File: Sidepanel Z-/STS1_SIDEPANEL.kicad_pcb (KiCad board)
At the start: 2 copper layers, 98 x 98 mm, 62 parts, among them IC1 TMP112AQDRLRQ1, J1 Conn_01x08, J3 Conn_02x02_Odd_Even, U1 GUVA-C32SM, U11 INA180A4, U12 INA180A4

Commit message: added the flex pcb
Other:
- board text removed: "C1"
- board text removed: "C2"
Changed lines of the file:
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@@
     (property "Sheetname" "SolarMPPT")
     (attr smd)
-    (fp_text reference "L_IN1" (at 0 0 270) (layer "B.SilkS")
+    (fp_text reference "L_IN1" (at 0 0) (layer "B.SilkS")
       (effects (font (size 1.27 1.27) (thickness 0.254)) (justify mirror))
     )
@@
     (property "Sheetname" "SolarMPPT")
     (attr smd)
-    (fp_text reference "RF12" (at 0 -3.25) (layer "B.SilkS")
+    (fp_text reference "RF12" (at -0.2162 -3.25) (layer "B.SilkS")
       (effects (font (size 1 1) (thickness 0.15)) (justify mirror))
     )
@@
     (property "Sheetname" "Sensors")
     (attr smd)
-    (fp_text reference "C1" (at 0 1.43) (layer "B.SilkS")
+    (fp_text reference "C1" (at 2.516 0.0784) (layer "B.SilkS")
       (effects (font (size 1 1) (thickness 0.15)) (justify mirror))
     )
@@
     (property "Sheetname" "Sensors")
     (attr smd)
-    (fp_text reference "C2" (at 0 -2.25) (layer "B.SilkS")
+    (fp_text reference "C2" (at -2.516 0.1286) (layer "B.SilkS")
       (effects (font (size 1 1) (thickness 0.15)) (justify mirror))
     )
@@
     (property "Sheetname" "Sensors")
     (attr smd)
-    (fp_text reference "IC1" (at 0 1.7 180) (layer "B.SilkS")
+    (fp_text reference "IC1" (at -0.0776 1.7796 180) (layer "B.SilkS")
       (effects (font (size 1 1) (thickness 0.15)) (justify mirror))
     )
@@
     (property "Sheetname" "SolarMPPT")
     (attr smd)
-    (fp_text reference "RF22" (at 0.237258 -3.75) (layer "B.SilkS")
+    (fp_text reference "RF22" (at -0.267 -3.5992) (layer "B.SilkS")
       (effects (font (size 1 1) (thickness 0.15)) (justify mirror))
     )
@@
     (property "Sheetname" "SolarMPPT")
     (attr smd)
-    (fp_text reference "DOUT2" (at -0.702 3.719) (layer "B.SilkS")
+    (fp_text reference "DOUT2" (at 0.055 -2.0756) (layer "B.SilkS")
       (effects (font (size 1.27 1.27) (thickness 0.254)) (justify mirror))
     )
@@
     (property "Sheetname" "SolarMPPT")
     (attr smd)
-    (fp_text reference "R51" (at 0 1.43) (layer "B.SilkS")
+    (fp_text reference "R51" (at 2.5908 0) (layer "B.SilkS")
       (effects (font (size 1 1) (thickness 0.15)) (justify mirror))
     )
@@
     (property "Sheetname" "SolarMPPT")
     (attr smd)
-    (fp_text reference "COUT12" (at 0 -3) (layer "B.SilkS")
+    (fp_text reference "COUT12" (at 0.0454 -1.9004) (layer "B.SilkS")
       (effects (font (size 1 1) (thickness 0.15)) (justify mirror))
     )
@@
     (property "Sheetname" "SolarMPPT")
     (attr smd)
-    (fp_text reference "CF2" (at 3.25 0 90) (layer "B.SilkS")
+    (fp_text reference "CF2" (at 3.158 0.4334 90) (layer "B.SilkS")
       (effects (font (size 1 1) (thickness 0.15)) (justify mirror))
     )
@@
     (property "Sheetname" "SolarMPPT")
     (attr smd)
-    (fp_text reference "C_CUR21" (at 5 0 90) (layer "B.SilkS")
+    (fp_text reference "C_CUR21" (at -5.2448 0.1302 90) (layer "B.SilkS")
       (effects (font (size 1 1) (thickness 0.15)) (justify mirror))
     )
@@
     (property "Sheetname" "SolarMPPT")
     (attr smd)
-    (fp_text reference "DOUT1" (at -0.702 3.719 180) (layer "B.SilkS")
+    (fp_text reference "DOUT1" (at 1.5078 -2.0832 180) (layer "B.SilkS")
       (effects (font (size 1.27 1.27) (thickness 0.254)) (justify mirror))
     )
@@
     (property "Sheetname" "SolarMPPT")
     (attr smd)
-    (fp_text reference "MPPT1" (at 0 2.45 180) (layer "B.SilkS")
+    (fp_text reference "MPPT1" (at 0.1034 -1.8788 180) (layer "B.SilkS")
       (effects (font (size 1 1) (thickness 0.15)) (justify mirror))
     )
@@
     (property "Sheetname" "SolarMPPT")
     (attr smd)
-    (fp_text reference "C_CUR12" (at -5 0 90) (layer "B.SilkS")
+    (fp_text reference "C_CUR12" (at -1.4932 1.5748 90) (layer "B.SilkS")
       (effects (font (size 1 1) (thickness 0.15)) (justify mirror))
     )
@@
     (property "Sheetname" "SolarMPPT")
     (attr smd)
-    (fp_text reference "CF1" (at 3.25 0 90) (layer "B.SilkS")
+    (fp_text reference "CF1" (at 2.7948 0.2738 90) (layer "B.SilkS")
       (effects (font (size 1 1) (thickness 0.15)) (justify mirror))
     )
@@
     (property "Sheetname" "SolarMPPT")
     (attr smd)
-    (fp_text reference "RF21" (at 0.237258 -3.75) (layer "B.SilkS")
+    (fp_text reference "RF21" (at -0.071 -3.6424) (layer "B.SilkS")
       (effects (font (size 1 1) (thickness 0.15)) (justify mirror))
     )
@@
     (property "Sheetname" "SolarMPPT")
     (attr smd)
-    (fp_text reference "C_IN2" (at 0.75 -1.5 90) (layer "B.SilkS")
+    (fp_text reference "C_IN2" (at 0.4784 -1.4446 90) (layer "B.SilkS")
       (effects (font (size 1 1) (thickness 0.15)) (justify mirror))
     )
@@
     (property "Sheetname" "SolarMPPT")
     (attr smd)
-    (fp_text reference "C_42" (at 0 1.43) (layer "B.SilkS")
+    (fp_text reference "C_42" (at -0.147 -1.5256) (layer "B.SilkS")
       (effects (font (size 1 1) (thickness 0.15)) (justify mirror))
     )
@@
     (property "Sheetname" "SolarMPPT")
     (attr smd)
-    (fp_text reference "C_CUR11" (at -5 0 90) (layer "B.SilkS")
+    (fp_text reference "C_CUR11" (at 5.2956 -0.0006 90) (layer "B.SilkS")
       (effects (font (size 1 1) (thickness 0.15)) (justify mirror))
     )
@@
     (property "Sheetname" "SolarMPPT")
     (attr smd)
-    (fp_text reference "L_IN2" (at 0 0 90) (layer "B.SilkS")
+    (fp_text reference "L_IN2" (at 0 0 180) (layer "B.SilkS")
       (effects (font (size 1.27 1.27) (thickness 0.254)) (justify mirror))
     )
@@
     (property "Sheetname" "SolarMPPT")
     (attr smd)
-    (fp_text reference "CUR1" (at 0 3.4 180) (layer "B.SilkS")
+    (fp_text reference "CUR1" (at -0.0326 -0.3084 270) (layer "B.SilkS")
       (effects (font (size 1 1) (thickness 0.15)) (justify mirror))
     )
@@
     (property "Sheetname" "SolarMPPT")
     (attr smd)
-    (fp_text reference "R31" (at 0 1.43) (layer "B.SilkS")
+    (fp_text reference "R31" (at 0.0074 -1.5688) (layer "B.SilkS")
       (effects (font (size 1 1) (thickness 0.15)) (justify mirror))
     )
@@
     (property "Sheetname" "SolarMPPT")
     (attr smd)
-    (fp_text reference "MPPT2" (at 0 2.45) (layer "B.SilkS")
+    (fp_text reference "MPPT2" (at 0.0962 -0.144) (layer "B.SilkS")
       (effects (font (size 1 1) (thickness 0.15)) (justify mirror))
     )
@@
     (property "Sheetname" "")
     (attr smd)
-    (fp_text reference "J1" (at -2.65 4.43 180) (layer "B.SilkS")
+    (fp_text reference "J1" (at -3.0988 3.9844 180) (layer "B.SilkS")
       (effects (font (size 1 1) (thickness 0.15)) (justify mirror))
     )
@@
     (property "Sheetname" "SolarMPPT")
     (attr smd)
-    (fp_text reference "R32" (at 0 1.43) (layer "B.SilkS")
+    (fp_text reference "R32" (at -0.0362 -1.6272) (layer "B.SilkS")
       (effects (font (size 1 1) (thickness 0.15)) (justify mirror))
     )
@@
     (property "Sheetname" "SolarMPPT")
     (attr smd)
-    (fp_text reference "RS2" (at 0 3.25) (layer "B.SilkS")
-      (effects (font (size 1 1) (thickness 0.15)) (justify mirror))
+    (fp_text reference "RS2" (at -0.0962 -1.1756) (layer "B.SilkS")
+      (effects (font (size 0.9 0.9) (thickness 0.15)) (justify mirror))
     )
     (fp_text value "0R01" (at 0 -1.43) (layer "B.Fab")
@@
     (property "Sheetname" "SolarMPPT")
     (attr smd)
-    (fp_text reference "C_41" (at 0 1.43) (layer "B.SilkS")
-      (effects (font (size 1 1) (thickness 0.15)) (justify mirror))
+    (fp_text reference "C_41" (at 0.9634 -2.1276 90) (layer "B.SilkS")
+      (effects (font (size 0.9 0.9) (thickness 0.15)) (justify mirror))
     )
     (fp_text value "100n" (at 0 -1.43) (layer "B.Fab")
@@
     (property "Sheetname" "SolarMPPT")
     (attr smd)
-    (fp_text reference "C_CUR22" (at 5 0 90) (layer "B.SilkS")
+    (fp_text reference "C_CUR22" (at 1.4424 1.6002 90) (layer "B.SilkS")
       (effects (font (size 1 1) (thickness 0.15)) (justify mirror))
     )
@@
   (gr_arc (start 130.5 89) (mid 131.707107 89.5) (end 130.5 90) (layer "Edge.Cuts") (width 0.1))
   (gr_arc (start 119.5 90) (mid 118.292893 89.5) (end 119.5 89) (layer "Edge.Cuts") (width 0.1))
-  (gr_text "C2" (at 101.25 104.25 -180) (layer "B.SilkS")
-    (effects (font (size 1 1) (thickness 0.15)) (justify mirror))
-  )
   (gr_text "Z-" (at 86.9 42.51) (layer "B.SilkS")
     (effects (font (size 1 1) (thickness 0.15)))
   )
-  (gr_text "C1" (at 97 104.18) (layer "B.SilkS")
-    (effects (font (size 1 1) (thickness 0.15)) (justify mirror))
-  )
   (gr_text "98 mm x 98 mm" (at 108.49 38.192) (layer "F.SilkS")

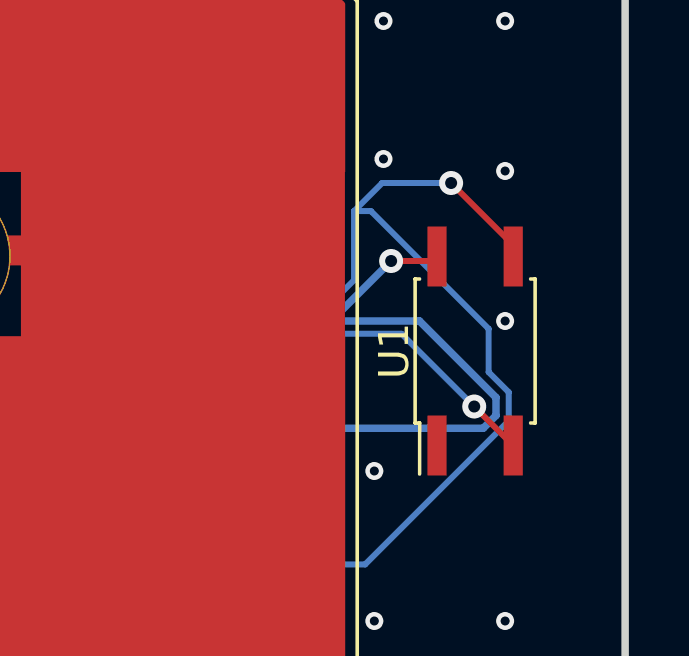
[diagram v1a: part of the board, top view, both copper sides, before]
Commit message: fix for the issues: #19, #18 moved some components from the edge away to avoid collisions with the new structure
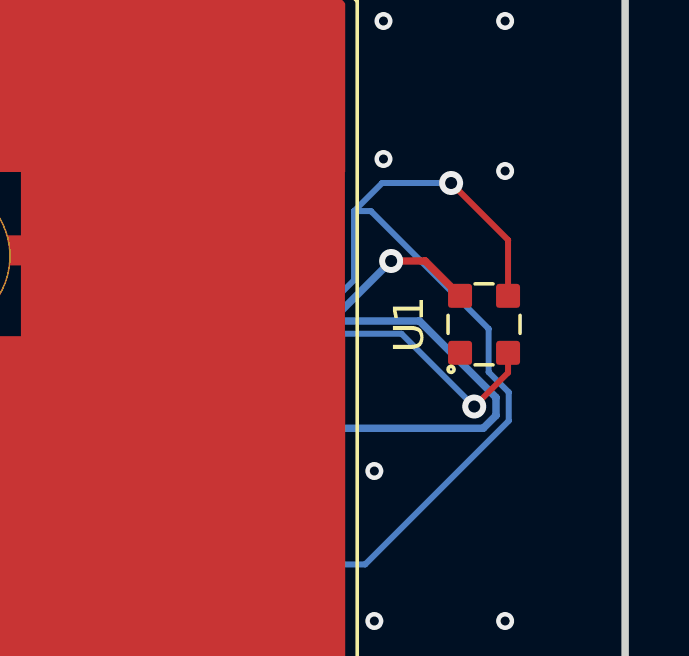
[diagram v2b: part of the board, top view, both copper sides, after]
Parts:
- U1: footprint Package_SO:SO-4_4.4x3.6mm_P2.54mm -> STS_UV:OLGA 2mm x 2,3mm
- moved U1 0.94 mm to (169.3, 69.6)
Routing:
- net /SCL: track 69.6 -> 70.8 mm
- net /+3V3: track 63.0 -> 64.2 mm
- net GND: vias 110 -> 109
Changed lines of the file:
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@@
     )
   )
-  (footprint "Package_SO:SO-4_4.4x3.6mm_P2.54mm" (layer "F.Cu")
-    (at 169 70.5 90)
-    (descr "4-Lead Plastic Small Outline (SO), see https://www.elpro.org/de/index.php?controller=attachment&id_attachment=339")
-    (tags "SO SOIC 2.54")
+  (footprint "STS_UV:OLGA 2mm x 2,3mm" (layer "F.Cu")
+    (at 169.2976 69.6118 90)
     (property "Sheetfile" "Sensors.kicad_sch")
     (property "Sheetname" "Sensors")
     (attr smd)
-    (fp_text reference "U1" (at 0 -2.7 90) (layer "F.SilkS")
+    (fp_text reference "U1" (at 0 -2.5 90 unlocked) (layer "F.SilkS")
       (effects (font (size 1 1) (thickness 0.15)))
     )
-    (fp_text value "GUVA-C32SM" (at 0 2.8 90) (layer "F.Fab")
+    (fp_text value "GUVA-C32SM" (at 0 2.5 90 unlocked) (layer "F.Fab")
       (effects (font (size 1 1) (thickness 0.15)))
     )
-    (fp_text user "${REFERENCE}" (at 0 -0.065 90) (layer "F.Fab")
+    (fp_text user "${REFERENCE}" (at 0.2 5.6 90 unlocked) (layer "F.Fab") hide
       (effects (font (size 1 1) (thickness 0.15)))
     )
-    (fp_line (start 2.4 -2) (end 2.4 -1.85) (layer "F.SilkS") (width 0.12))
-    (fp_line (start 2.4 2) (end -2.4 2) (layer "F.SilkS") (width 0.12))
-    (fp_line (start 2.4 1.85) (end 2.4 2) (layer "F.SilkS") (width 0.12))
-    (fp_line (start -2.4 -2) (end 2.4 -2) (layer "F.SilkS") (width 0.12))
-    (fp_line (start -2.4 -1.85) (end -2.4 -2) (layer "F.SilkS") (width 0.12))
-    (fp_line (start -2.4 2) (end -2.4 1.85) (layer "F.SilkS") (width 0.12))
-    (fp_line (start -2.4 -1.85) (end -4.1 -1.85) (layer "F.SilkS") (width 0.12))
-    (fp_line (start -4.4 -2.05) (end 4.4 -2.05) (layer "F.CrtYd") (width 0.05))
-    (fp_line (start 4.4 2.05) (end 4.4 -2.05) (layer "F.CrtYd") (width 0.05))
-    (fp_line (start 4.4 2.05) (end -4.4 2.05) (layer "F.CrtYd") (width 0.05))
-    (fp_line (start -4.4 -2.05) (end -4.4 2.05) (layer "F.CrtYd") (width 0.05))
-    (fp_line (start 2.2 -1.8) (end 2.2 1.8) (layer "F.Fab") (width 0.12))
-    (fp_line (start -1.4 -1.8) (end 2.2 -1.8) (layer "F.Fab") (width 0.12))
-    (fp_line (start -2.2 1.8) (end -2.2 -1) (layer "F.Fab") (width 0.12))
-    (fp_line (start 2.2 1.8) (end -2.2 1.8) (layer "F.Fab") (width 0.12))
-    (fp_line (start -2.2 -1) (end -1.4 -1.8) (layer "F.Fab") (width 0.12))
-    (pad "1" smd rect (at -3.15 -1.27 90) (size 2 0.64) (layers "F.Cu" "F.Paste" "F.Mask")
+    (fp_line (start -0.3 -1.2) (end 0.3 -1.2) (layer "F.SilkS") (width 0.12))
+    (fp_line (start -1.35 0.3) (end -1.35 -0.3) (layer "F.SilkS") (width 0.12))
+    (fp_line (start 1.35 0.3) (end 1.35 -0.3) (layer "F.SilkS") (width 0.12))
+    (fp_line (start -0.3 1.2) (end 0.3 1.2) (layer "F.SilkS") (width 0.12))
+    (fp_circle (center -1.5 -1.1) (end -1.5 -1.2) (layer "F.SilkS") (width 0.12) (fill none))
+    (fp_line (start 1.6 -1.5) (end -1.6 -1.5) (layer "F.CrtYd") (width 0.05))
+    (fp_line (start -1.6 1.5) (end 1.6 1.5) (layer "F.CrtYd") (width 0.05))
+    (fp_line (start -1.6 1.5) (end -1.6 -1.5) (layer "F.CrtYd") (width 0.05))
+    (fp_line (start 1.6 -1.5) (end 1.6 1.5) (layer "F.CrtYd") (width 0.05))
+    (fp_line (start 1.15 1) (end 1.15 -1) (layer "F.Fab") (width 0.1))
+    (fp_line (start -0.6 0.3) (end 0.6 0.3) (layer "F.Fab") (width 0.1))
+    (fp_line (start -0.4 -0.3) (end -0.4 -0.5) (layer "F.Fab") (width 0.1))
+    (fp_line (start -0.2 -0.1) (end -0.2 0.7) (layer "F.Fab") (width 0.1))
+    (fp_line (start -1.15 1) (end 1.15 1) (layer "F.Fab") (width 0.1))
+    (fp_line (start 0.2 0.7) (end 0.2 -0.1) (layer "F.Fab") (width 0.1))
+    (fp_line (start -1.15 -1) (end -1.15 1) (layer "F.Fab") (width 0.1))
+    (fp_line (start -0.4 -0.3) (end -0.1 -0.6) (layer "F.Fab") (width 0.1))
+    (fp_line (start 0.1 -0.3) (end 0.1 -0.5) (layer "F.Fab") (width 0.1))
+    (fp_line (start -0.2 0.3) (end 0.2 0.7) (layer "F.Fab") (width 0.1))
+    (fp_line (start 0.2 -0.1) (end -0.2 0.3) (layer "F.Fab") (width 0.1))
+    (fp_line (start 1.15 -1) (end -1.15 -1) (layer "F.Fab") (width 0.1))
+    (fp_line (start 0.1 -0.3) (end 0.3 -0.3) (layer "F.Fab") (width 0.1))
+    (fp_line (start 0.1 -0.3) (end 0.4 -0.6) (layer "F.Fab") (width 0.1))
+    (fp_line (start -0.4 -0.3) (end -0.2 -0.3) (layer "F.Fab") (width 0.1))
+    (pad "1" smd roundrect (at -0.95 -0.8 270) (size 0.8 0.8) (layers "F.Cu" "F.Paste" "F.Mask") (roundrect_rratio 0.125)
       (net 1 "GND") (pinfunction "GND") (pintype "power_in"))
-    (pad "2" smd rect (at -3.15 1.27 90) (size 2 0.64) (layers "F.Cu" "F.Paste" "F.Mask")
+    (pad "2" smd roundrect (at -0.95 0.8 270) (size 0.8 0.8) (layers "F.Cu" "F.Paste" "F.Mask") (roundrect_rratio 0.125)
       (net 6 "/SDA") (pinfunction "SDA") (pintype "bidirectional"))
-    (pad "3" smd rect (at 3.15 1.27 90) (size 2 0.64) (layers "F.Cu" "F.Paste" "F.Mask")
+    (pad "3" smd roundrect (at 0.95 0.8 270) (size 0.8 0.8) (layers "F.Cu" "F.Paste" "F.Mask") (roundrect_rratio 0.125)
       (net 4 "/SCL") (pinfunction "SCL") (pintype "input"))
-    (pad "4" smd rect (at 3.15 -1.27 90) (size 2 0.64) (layers "F.Cu" "F.Paste" "F.Mask")
+    (pad "4" smd roundrect (at 0.95 -0.8 270) (size 0.8 0.8) (layers "F.Cu" "F.Paste" "F.Mask") (roundrect_rratio 0.125)
       (net 3 "/+3V3") (pinfunction "VCC") (pintype "power_in"))
-    (model "${KICAD6_3DMODEL_DIR}/Package_SO.3dshapes/SO-4_4.4x3.6mm_P2.54mm.wrl"
-      (offset (xyz 0 0 0))
-      (scale (xyz 1 1 1))
-      (rotate (xyz 0 0 0))
+    (model "C:/Users/Alex/Documents/KiCad/6.0/3dmodels/OLGA2x2,3.stp"
+      (offset (xyz 0 0 0))
+      (scale (xyz 1 1 1))
+      (rotate (xyz 90 -180 180))
     )
   )
@@
   (via (at 125 132.71) (size 0.6) (drill 0.3) (layers "F.Cu" "B.Cu") (free) (net 1))
   (via (at 165.64 74.5) (size 0.6) (drill 0.3) (layers "F.Cu" "B.Cu") (free) (net 1))
-  (via (at 170 69.5) (size 0.6) (drill 0.3) (layers "F.Cu" "B.Cu") (free) (net 1))
   (via (at 165.8 119.5) (size 0.6) (drill 0.3) (layers "F.Cu" "B.Cu") (free) (net 1))
   (via (at 165.9448 54.4988) (size 0.6) (drill 0.3) (layers "F.Cu" "B.Cu") (free) (net 1))
@@
   (segment (start 128.979521 85.920479) (end 122.279521 85.920479) (width 1) (layer "B.Cu") (net 2))
   (segment (start 122.279521 85.920479) (end 121 87.2) (width 1) (layer "B.Cu") (net 2))
-  (segment (start 167.58 67.5) (end 167.73 67.35) (width 0.2) (layer "F.Cu") (net 3))
-  (segment (start 166.2 67.5) (end 167.58 67.5) (width 0.2) (layer "F.Cu") (net 3))
+  (segment (start 167.3358 67.5) (end 168.4976 68.6618) (width 0.25) (layer "F.Cu") (net 3))
+  (segment (start 166.2 67.5) (end 167.3358 67.5) (width 0.25) (layer "F.Cu") (net 3))
   (via (at 166.2 67.5) (size 0.8) (drill 0.4) (layers "F.Cu" "B.Cu") (net 3))
   (segment (start 150.9 94.87) (end 148.9 94.87) (width 0.25) (layer "B.Cu") (net 3))
@@
   (segment (start 161.842 73.637) (end 161.842 76.709) (width 0.25) (layer "B.Cu") (net 3))
   (segment (start 152.65 89.1) (end 152.65 86.45) (width 0.25) (layer "B.Cu") (net 3))
-  (segment (start 170.27 66.97) (end 170.27 67.35) (width 0.2) (layer "F.Cu") (net 4))
-  (segment (start 168.2 64.9) (end 170.27 66.97) (width 0.2) (layer "F.Cu") (net 4))
+  (segment (start 170.0976 68.6618) (end 170.0976 66.8052) (width 0.2) (layer "F.Cu") (net 4))
+  (segment (start 168.2 64.9) (end 170.1014 66.8014) (width 0.2) (layer "F.Cu") (net 4))
+  (segment (start 170.0976 66.8052) (end 170.1014 66.8014) (width 0.2) (layer "F.Cu") (net 4))
   (via (at 168.2 64.9) (size 0.8) (drill 0.4) (layers "F.Cu" "B.Cu") (net 4))
   (segment (start 169.45 69.76005) (end 169.45 71.203655) (width 0.2) (layer "B.Cu") (net 4))
@@
   (segment (start 152.849158 83.82548) (end 157.850969 78.823669) (width 0.2) (layer "B.Cu") (net 4))
   (segment (start 149.511 84.423994) (end 150.109514 83.82548) (width 0.2) (layer "B.Cu") (net 4))
-  (segment (start 168.970489 72.350489) (end 170.27 73.65) (width 0.2) (layer "F.Cu") (net 6))
+  (segment (start 168.970489 72.350489) (end 170.0976 71.223378) (width 0.2) (layer "F.Cu") (net 6))
+  (segment (start 170.0976 71.223378) (end 170.0976 70.5618) (width 0.2) (layer "F.Cu") (net 6))
   (via (at 168.970489 72.350489) (size 0.8) (drill 0.4) (layers "F.Cu" "B.Cu") (net 6))
   (segment (start 166.54452 69.92452) (end 168.970489 72.350489) (width 0.2) (layer "B.Cu") (net 6))
